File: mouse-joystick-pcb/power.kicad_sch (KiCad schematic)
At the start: 10 parts, among them J301 2.1, U301 TPSM365R6V5RDNR

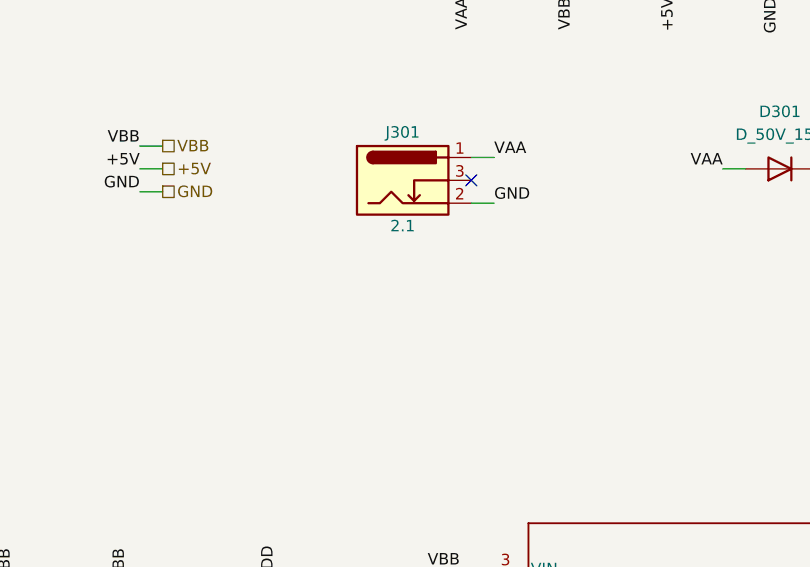
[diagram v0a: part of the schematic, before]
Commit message: Update documentation for future v1.1
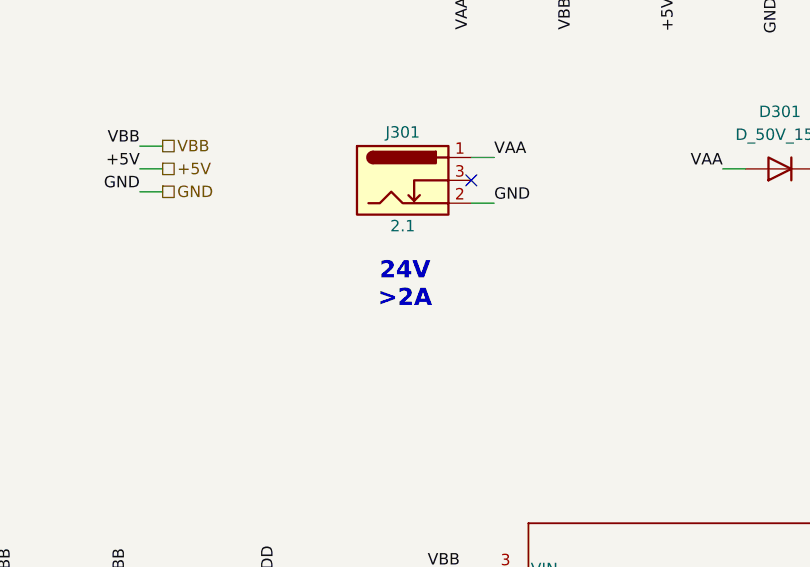
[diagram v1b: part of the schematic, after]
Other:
- note added: "24V >2A"
- company: Peter Polidoro -> Janelia Research Campus
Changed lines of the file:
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@@
 	(title_block
 		(title "mouse-joystick-pcb")
-		(date "2024-10-24")
-		(rev "1.0")
-		(company "Peter Polidoro")
+		(date "2026-01-15")
+		(rev "1.1")
+		(company "Janelia Research Campus")
+		(comment 1 "Peter Polidoro")
+	)
+	(text "24V\n>2A"
+		(exclude_from_sim no)
+		(at 123.444 80.264 0)
+		(effects
+			(font
+				(size 1.905 1.905)
+				(thickness 0.508)
+				(bold yes)
+			)
+		)
 	)
 	(no_connect
@@
 		(at 165.1 67.31 180)
 		(unit 1)
-		(exclude_from_sim yes)
+		(exclude_from_sim no)
 		(in_bom yes)
 		(on_board yes)
